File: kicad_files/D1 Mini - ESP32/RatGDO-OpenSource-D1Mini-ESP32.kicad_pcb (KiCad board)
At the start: 2 copper layers, 55 x 70 mm, 13 parts, among them J1 Screw_Terminal_01x03, J2 Screw_Terminal_01x03, J3 Screw_Terminal_01x03, Q1 2N7002, Q2 AO3400A, U1 mini_esp32

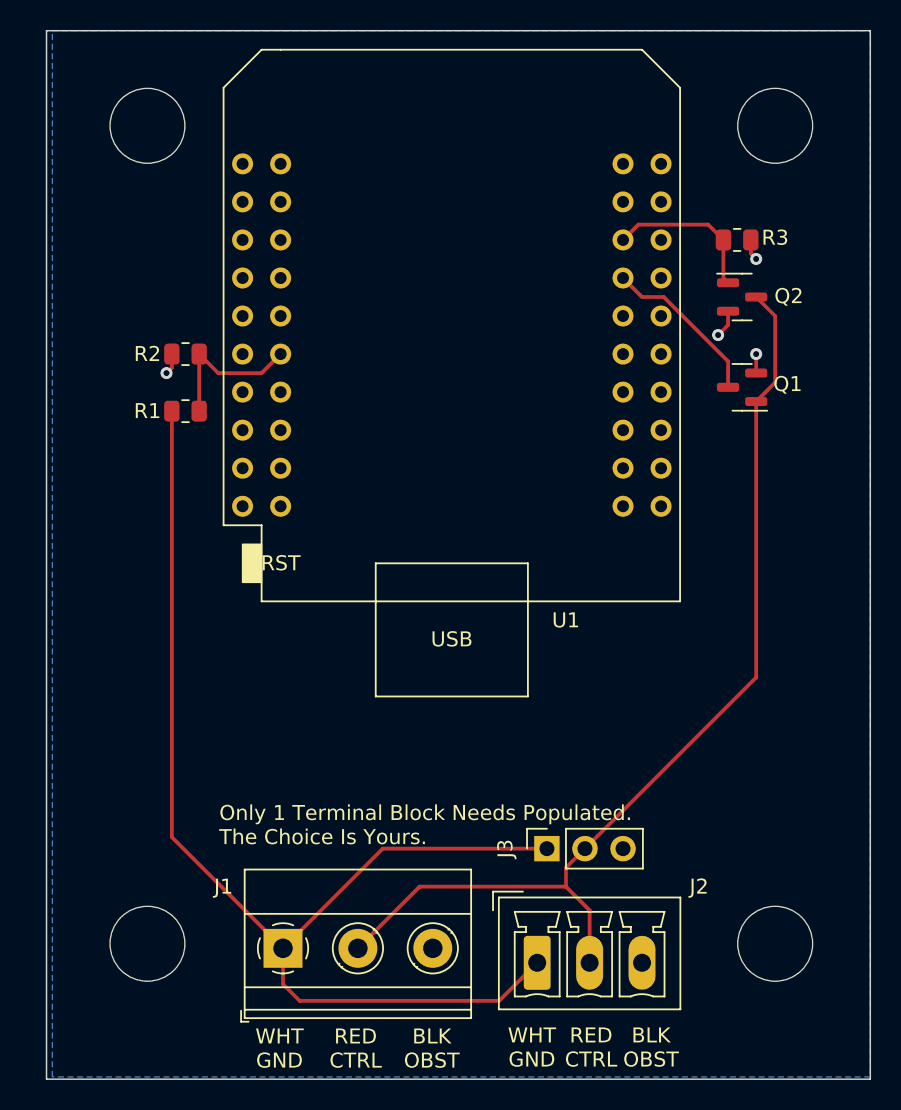
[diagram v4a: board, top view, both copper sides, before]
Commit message: ESP32 footprint did not properly create a keepout zone.
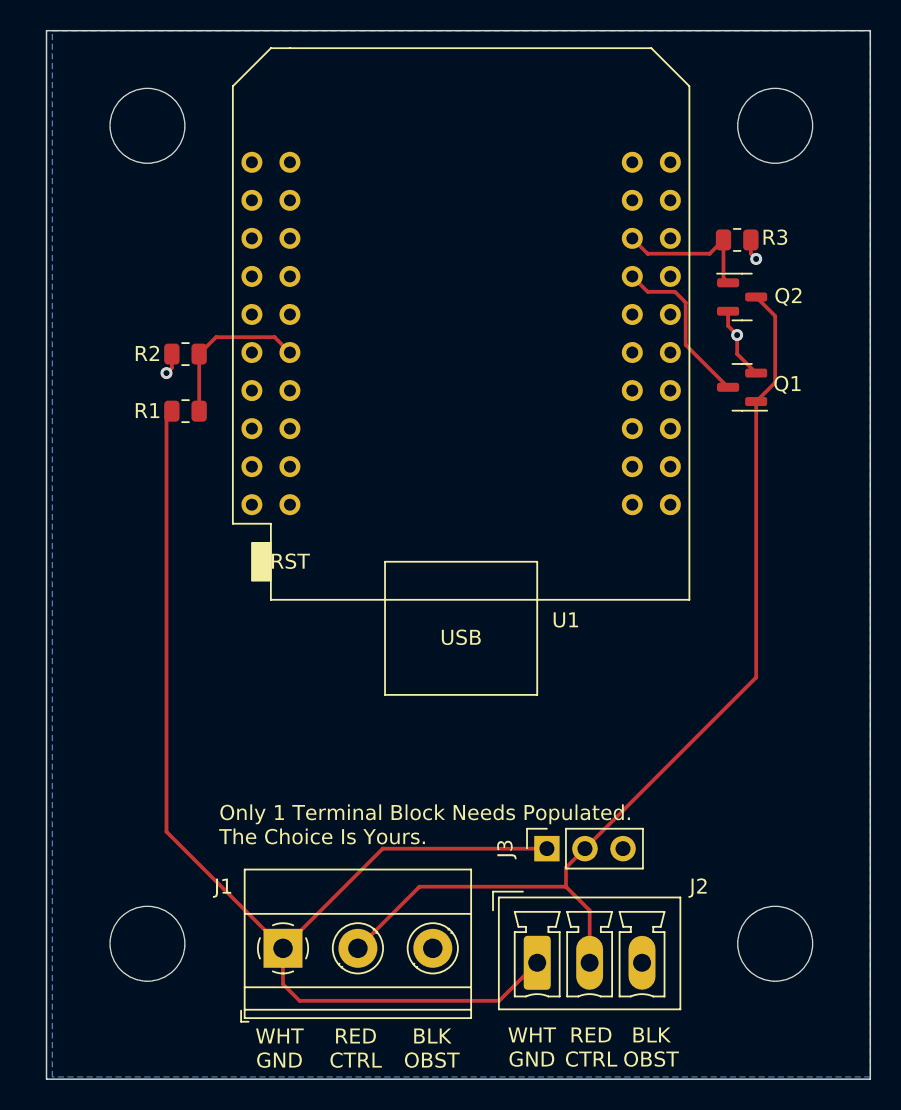
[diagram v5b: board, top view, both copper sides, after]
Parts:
- moved U1 0.63 mm to (141.6, 77.4)
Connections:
- U1 pad 12: Net-(U2-IO_23/D7) -> Net-(U1-IO_23/D7)
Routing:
- net Net-(U1-IO_23/D7): track 0.00 -> 10.8 mm
- net Net-(U2-IO_23/D7): track 10.3 -> 0.00 mm
- net GND: track 5.97 -> 7.74 mm, vias 4 -> 3
- net Net-(Q2-G): track 10.5 -> 9.88 mm

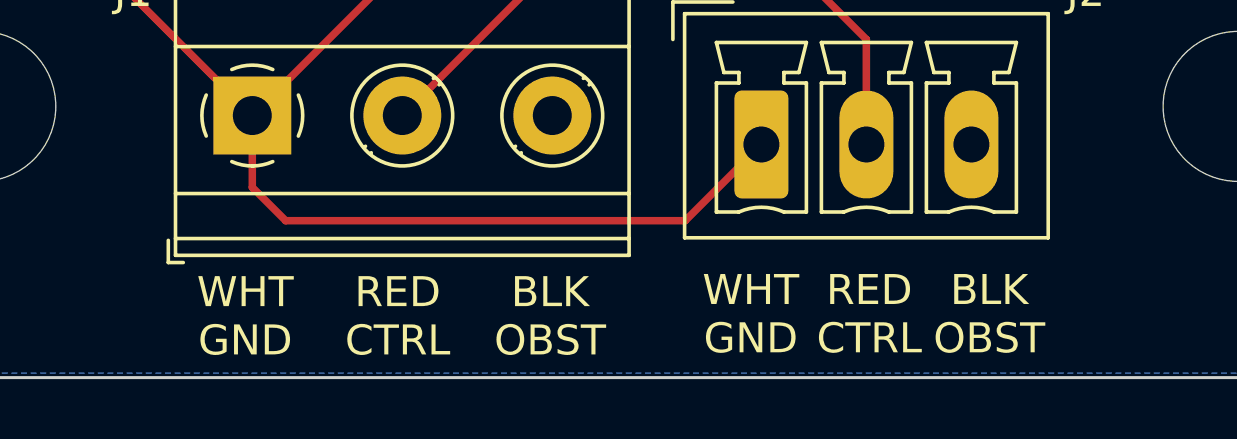
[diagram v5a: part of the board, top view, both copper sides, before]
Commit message: Fixed Silkscreen issue - positive and ground swap
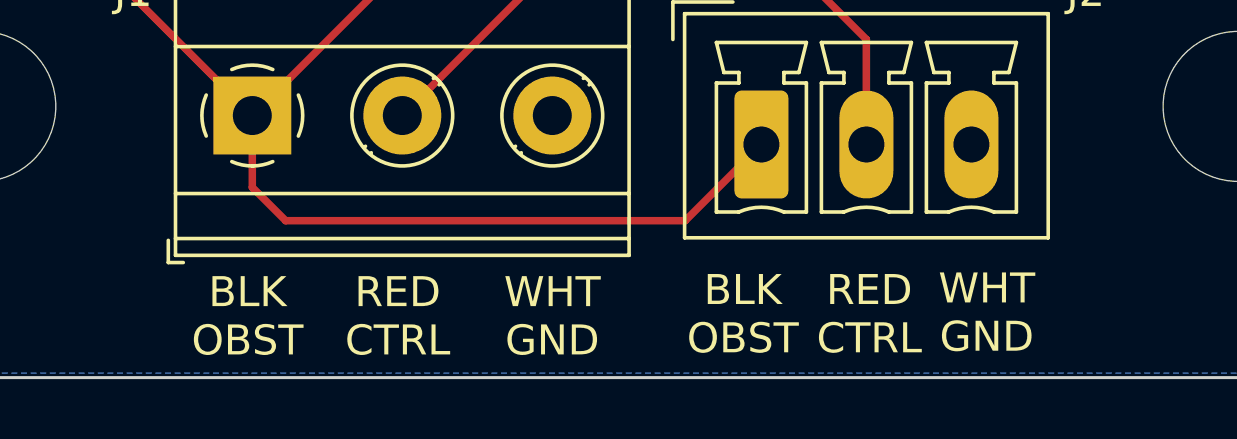
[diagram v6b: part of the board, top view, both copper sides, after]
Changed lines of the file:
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@@
     (effects (font (size 1 1) (thickness 0.15)) (justify left bottom mirror))
   )
-  (gr_text "BLK\nOBST" (at 154.265587 126.429201) (layer "F.SilkS")
+  (gr_text "BLK\nOBST" (at 146.05 126.429201) (layer "F.SilkS")
     (effects (font (size 1 1) (thickness 0.15)) (justify bottom))
   )
@@
     (effects (font (size 1 1) (thickness 0.15)) (justify bottom))
   )
-  (gr_text "WHT\nGND" (at 129.466103 126.499836) (layer "F.SilkS")
+  (gr_text "WHT\nGND" (at 139.7 126.499836) (layer "F.SilkS")
     (effects (font (size 1 1) (thickness 0.15)) (justify bottom))
   )
@@
     (effects (font (size 1 1) (thickness 0.15)) (justify left bottom))
   )
-  (gr_text "BLK\nOBST" (at 139.626103 126.499836) (layer "F.SilkS")
+  (gr_text "BLK\nOBST" (at 129.54 126.499836) (layer "F.SilkS")
     (effects (font (size 1 1) (thickness 0.15)) (justify bottom))
   )
-  (gr_text "WHT\nGND" (at 146.317376 126.429201) (layer "F.SilkS")
+  (gr_text "WHT\nGND" (at 154.183507 126.37723) (layer "F.SilkS")
     (effects (font (size 1 1) (thickness 0.15)) (justify bottom))
   )

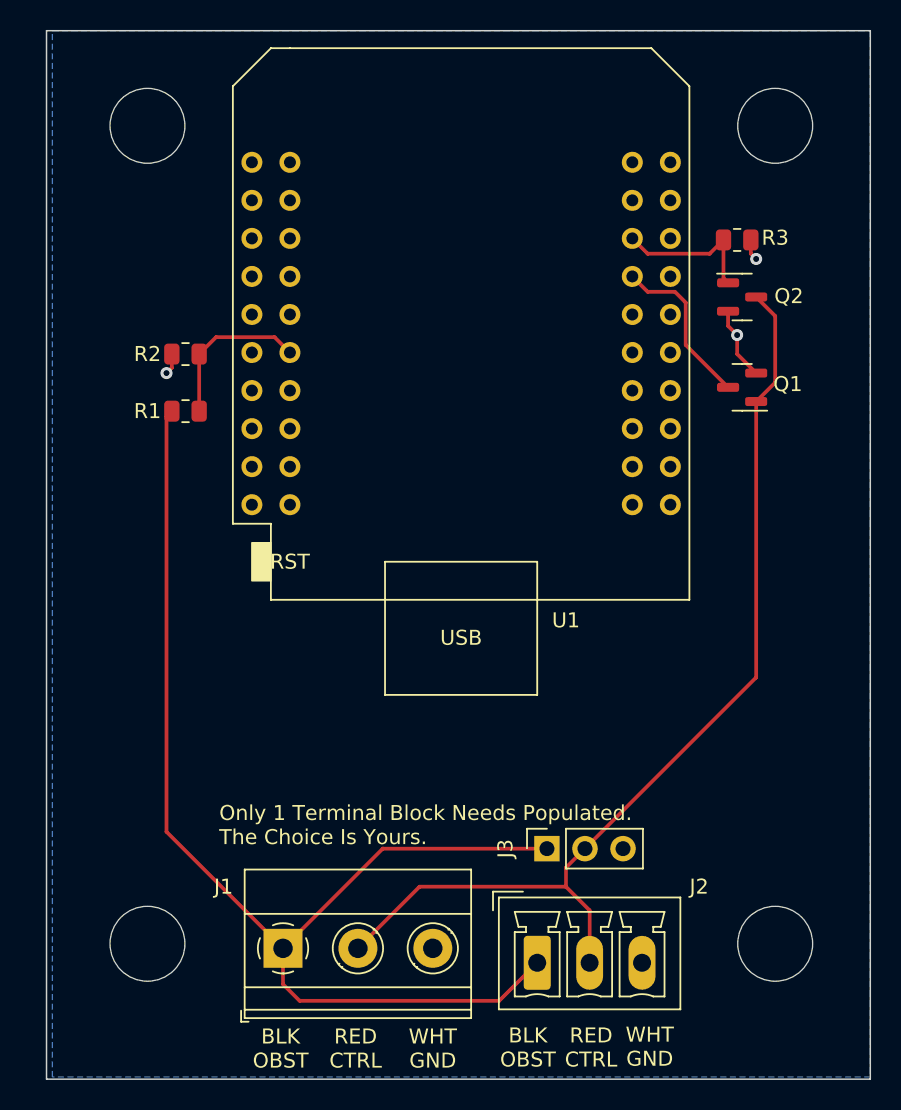
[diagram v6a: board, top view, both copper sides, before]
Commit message: Update ESP32 Mini schematics and PCB
Added 1K R4 on gate of Q2.
Added 10K R5/R6 on gate of Q1.
Re-laid out PCB, all single sided and smaller.
Changed pads to hand solder.
Modified from ESP8266 layout.
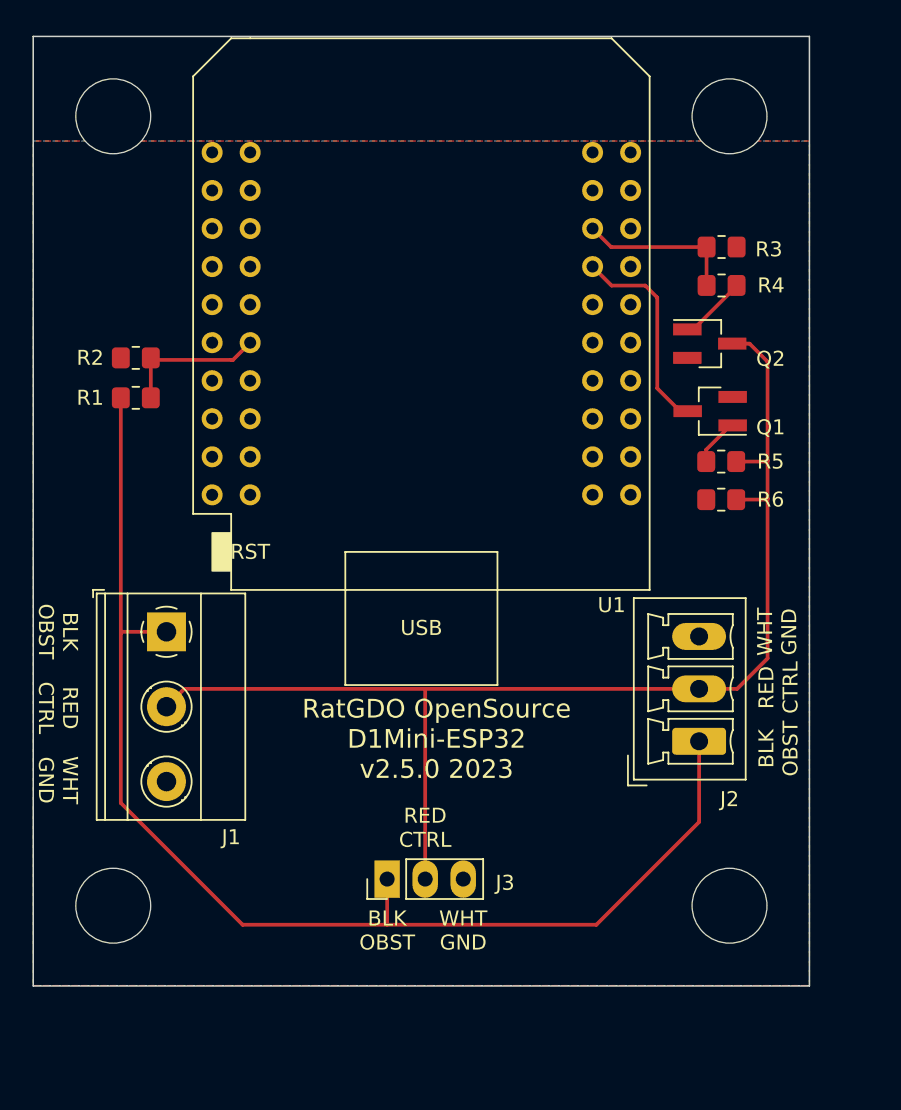
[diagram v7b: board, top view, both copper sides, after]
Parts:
- added R4: 1k, Resistor_SMD:R_0805_2012Metric_Pad1.20x1.40mm_HandSolder, F.Cu at (159.0, 74.2)
- added R5: 10k, Resistor_SMD:R_0805_2012Metric_Pad1.20x1.40mm_HandSolder, F.Cu at (159.0, 85.9)
- added R6: 10k, Resistor_SMD:R_0805_2012Metric_Pad1.20x1.40mm_HandSolder, F.Cu at (159.0, 88.5)
- J3: footprint Connector_PinSocket_2.54mm:PinSocket_1x03_P2.54mm_Vertical -> Connector_PinHeader_2.54mm:PinHeader_1x03_P2.54mm_Vertical
- Q1, Q2: footprint Package_TO_SOT_SMD:SOT-23 -> Package_TO_SOT_SMD:SOT-23_Handsoldering
- R1, R2, R3: footprint Resistor_SMD:R_0805_2012Metric -> Resistor_SMD:R_0805_2012Metric_Pad1.20x1.40mm_HandSolder
- moved J1 22.5 mm to (121.9, 97.3), turned to -90 degrees
- moved J2 18.3 mm to (157.5, 104.6), turned to 90 degrees
- moved J3 10.9 mm to (136.7, 113.8)
- moved REF** 3.97 mm to (159.5, 115.6)
- moved Q2 3.79 mm to (158.2, 78.0)
- moved R1 3.44 mm to (119.9, 81.7)
- moved REF** 3.42 mm to (118.4, 115.6)
- moved R2 3.33 mm to (119.9, 79.0)
- moved REF** 3.11 mm to (159.5, 62.9)
- moved U1 2.73 mm to (138.9, 76.7)
- moved Q1 2.66 mm to (158.2, 82.5)
- moved REF** 2.37 mm to (118.4, 62.9)
- moved R3 1.14 mm to (159.0, 71.6), turned to 0 degrees
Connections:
- net Net-(J1-BLK/OBST) renamed BLK/OBST
- net Net-(Q1-D) renamed /ESP_RX
- J1 pad 2: Net-(J1-RED/CTRL) -> RED/CTRL
- J2 pad 2: Net-(J1-RED/CTRL) -> RED/CTRL
- J3 pad 2: Net-(J1-RED/CTRL) -> RED/CTRL
- Q1 pad 1: Net-(J1-RED/CTRL) -> Net-(Q1-G)
- Q2 pad 3: Net-(J1-RED/CTRL) -> RED/CTRL
- R3 pad 1: GND -> /ESP_TX
- R3 pad 2: Net-(Q2-G) -> GND
- U1 pad 1: unconnected-(U1-GND-Pad1) -> GND
- U1 pad 22: unconnected-(U1-GND-Pad22) -> GND
- U1 pad 25: Net-(Q2-G) -> /ESP_TX
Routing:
- net RED/CTRL: track 0.00 -> 81.1 mm
- net Net-(J1-RED/CTRL): track 67.0 -> 0.00 mm
- net /ESP_TX: track 0.00 -> 10.6 mm
- net GND: track 7.74 -> 0.00 mm, vias 3 -> 0
- net Net-(Q2-G): track 9.88 -> 4.08 mm
- net Net-(Q1-G): track 0.00 -> 3.09 mm
- net BLK/OBST: track 80.5 -> 83.1 mm
- net /ESP_RX: track 11.1 -> 13.4 mm
- net Net-(U1-IO_23/D7): track 10.8 -> 9.64 mm
- added copper zone on F.Cu, net GND
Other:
- board size 55 x 70 mm -> 51.8 x 63.4 mm
- board text added: "3V3"
- board text added: "CLK"
- board text added: "CMD"
- board text added: "IO0"
- board text added: "IO16"
- board text added: "IO17"
- board text added: "IO18"
- board text added: "IO19"
- board text added: "IO2"
- board text added: "IO21"
- board text added: "IO22"
- board text added: "IO23"
- board text added: "IO25"
- board text added: "IO26"
- board text added: "IO27"
- board text added: "IO32"
- board text added: "IO33"
- board text added: "IO34"
- board text added: "IO35"
- board text added: "IO4"
- board text added: "IO5"
- board text added: "NC"
- board text added: "Only 1 Terminal Block Needs Populating. The Choice Is Yours."
- board text added: "RXD"
- board text added: "RatGDO OpenSource D1Mini-ESP32 v2.5.0 2023"
- board text added: "SD1"
- board text added: "SD2"
- board text added: "SD3"
- board text added: "SDO"
- board text added: "SVN"
- board text added: "SVP"
- board text added: "TCK"
- board text added: "TDI"
- board text added: "TDO"
- board text added: "TMS"
- board text added: "TXD"
- board text added: "VCC"
- board text removed: "5v"
- board text removed: "EN"
- board text removed: "GPIO16"
- board text removed: "GPIO17"
- board text removed: "GPIO18"
- board text removed: "GPIO19"
- board text removed: "GPIO21"
- board text removed: "GPIO22"
- board text removed: "GPIO23"
- board text removed: "GPIO26"
- board text removed: "GPIO5"
- board text removed: "Only 1 Terminal Block Needs Populated. The Choice Is Yours."
- board text removed: "RX"
- board text removed: "TX"
- board text removed: "VCC-3v3"

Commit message: Update schematics for mini wide board v2.5
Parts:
- renumbered REF** to H1
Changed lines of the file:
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@@
     (descr "Mounting Hole 5mm, no annular")
     (tags "mounting hole 5mm no annular")
-    (attr exclude_from_pos_files exclude_from_bom)
-    (fp_text reference "REF**" (at 0 -6) (layer "F.SilkS") hide
+    (attr board_only exclude_from_pos_files exclude_from_bom)
+    (fp_text reference "H1" (at 0 -6) (layer "F.SilkS") hide
         (effects (font (size 1 1) (thickness 0.15)))
     )
@@
     (descr "Mounting Hole 5mm, no annular")
     (tags "mounting hole 5mm no annular")
-    (attr exclude_from_pos_files exclude_from_bom)
-    (fp_text reference "REF**" (at 0 -6) (layer "F.SilkS") hide
+    (attr board_only exclude_from_pos_files exclude_from_bom)
+    (fp_text reference "H1" (at 0 -6) (layer "F.SilkS") hide
         (effects (font (size 1 1) (thickness 0.15)))
     )
@@
     (descr "Mounting Hole 5mm, no annular")
     (tags "mounting hole 5mm no annular")
-    (attr exclude_from_pos_files exclude_from_bom)
-    (fp_text reference "REF**" (at 0 -6) (layer "F.SilkS") hide
+    (attr board_only exclude_from_pos_files exclude_from_bom)
+    (fp_text reference "H1" (at 0 -6) (layer "F.SilkS") hide
         (effects (font (size 1 1) (thickness 0.15)))
     )
@@
     (descr "Mounting Hole 5mm, no annular")
     (tags "mounting hole 5mm no annular")
-    (attr exclude_from_pos_files exclude_from_bom)
-    (fp_text reference "REF**" (at 0 -6) (layer "F.SilkS") hide
-        (effects (font (size 1 1) (thickness 0.15)))
-    )
+    (attr board_only exclude_from_pos_files exclude_from_bom)
+    (fp_text reference "H1" (at 0 -6) (layer "F.SilkS") hide
+        (effects (font (size 1 1) (thickness 0.15)))
+    )
